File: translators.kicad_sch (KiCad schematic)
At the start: 22 parts

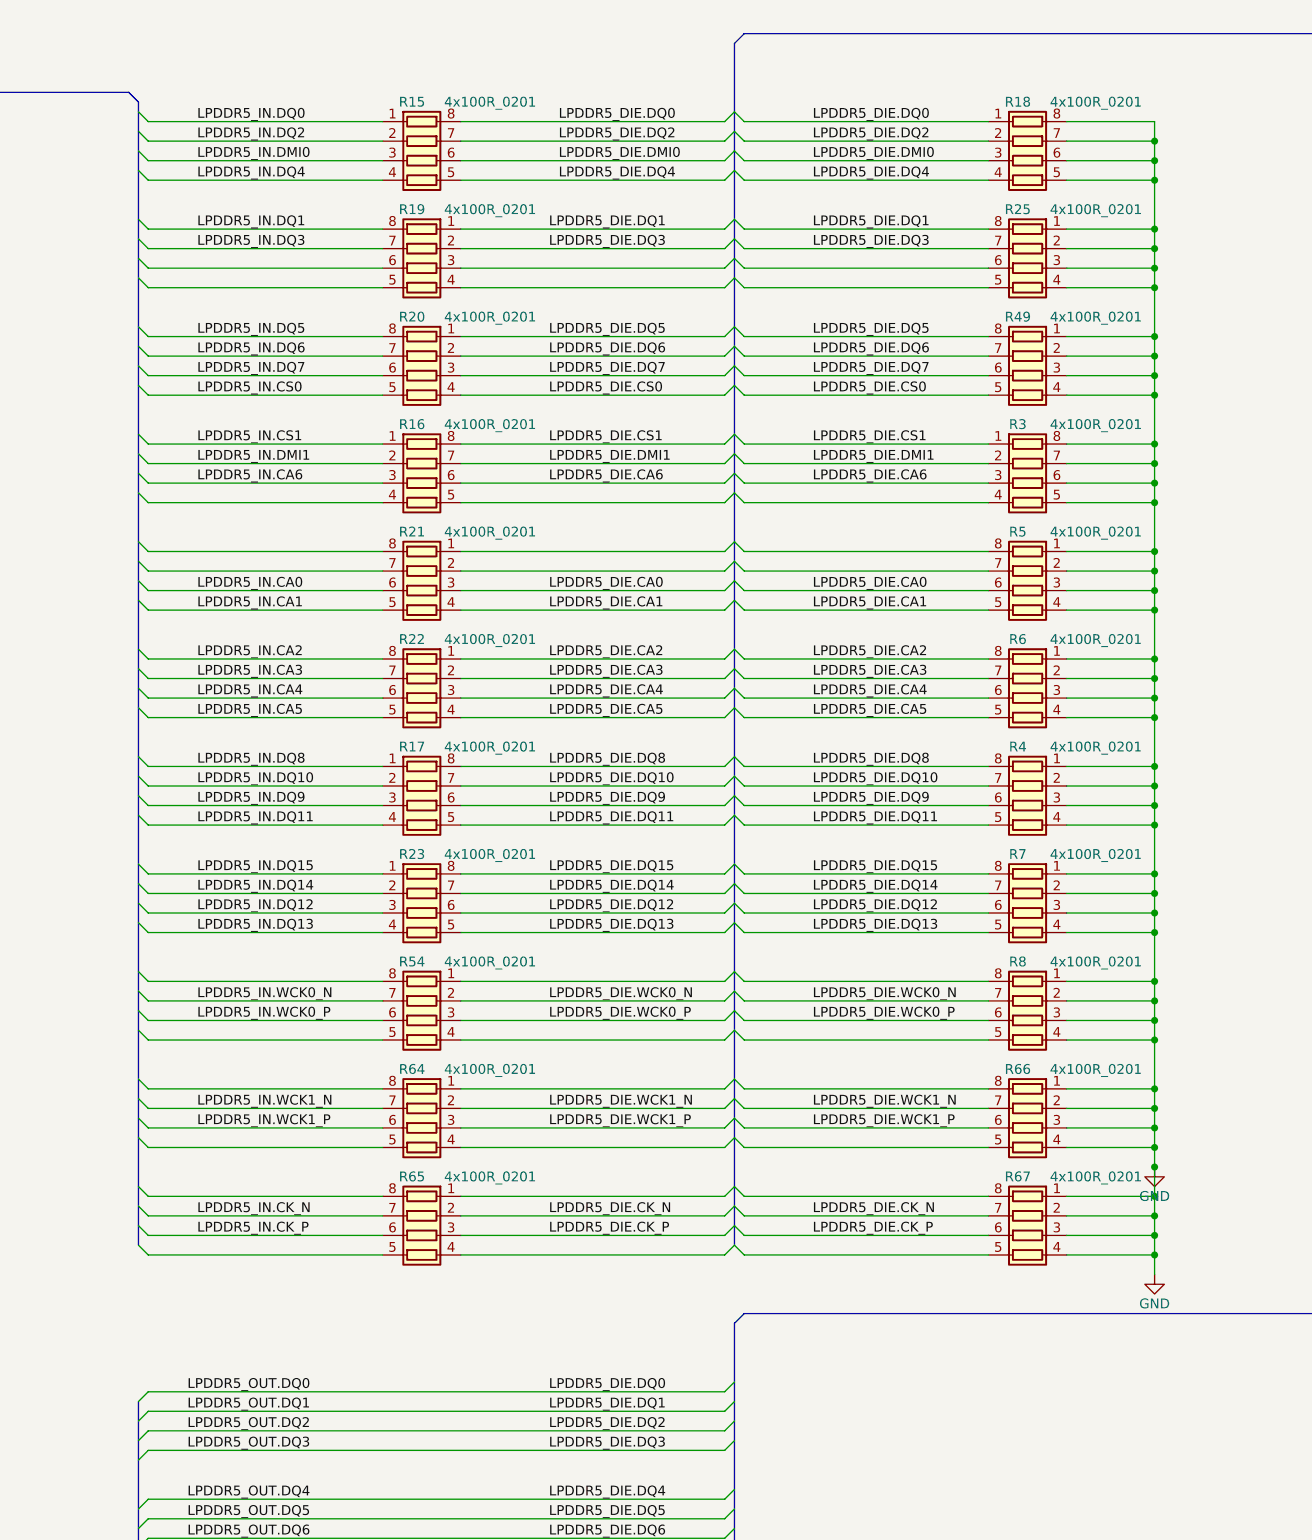
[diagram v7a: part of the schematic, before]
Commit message: [#52835] schematics: replace array resistors with 0402
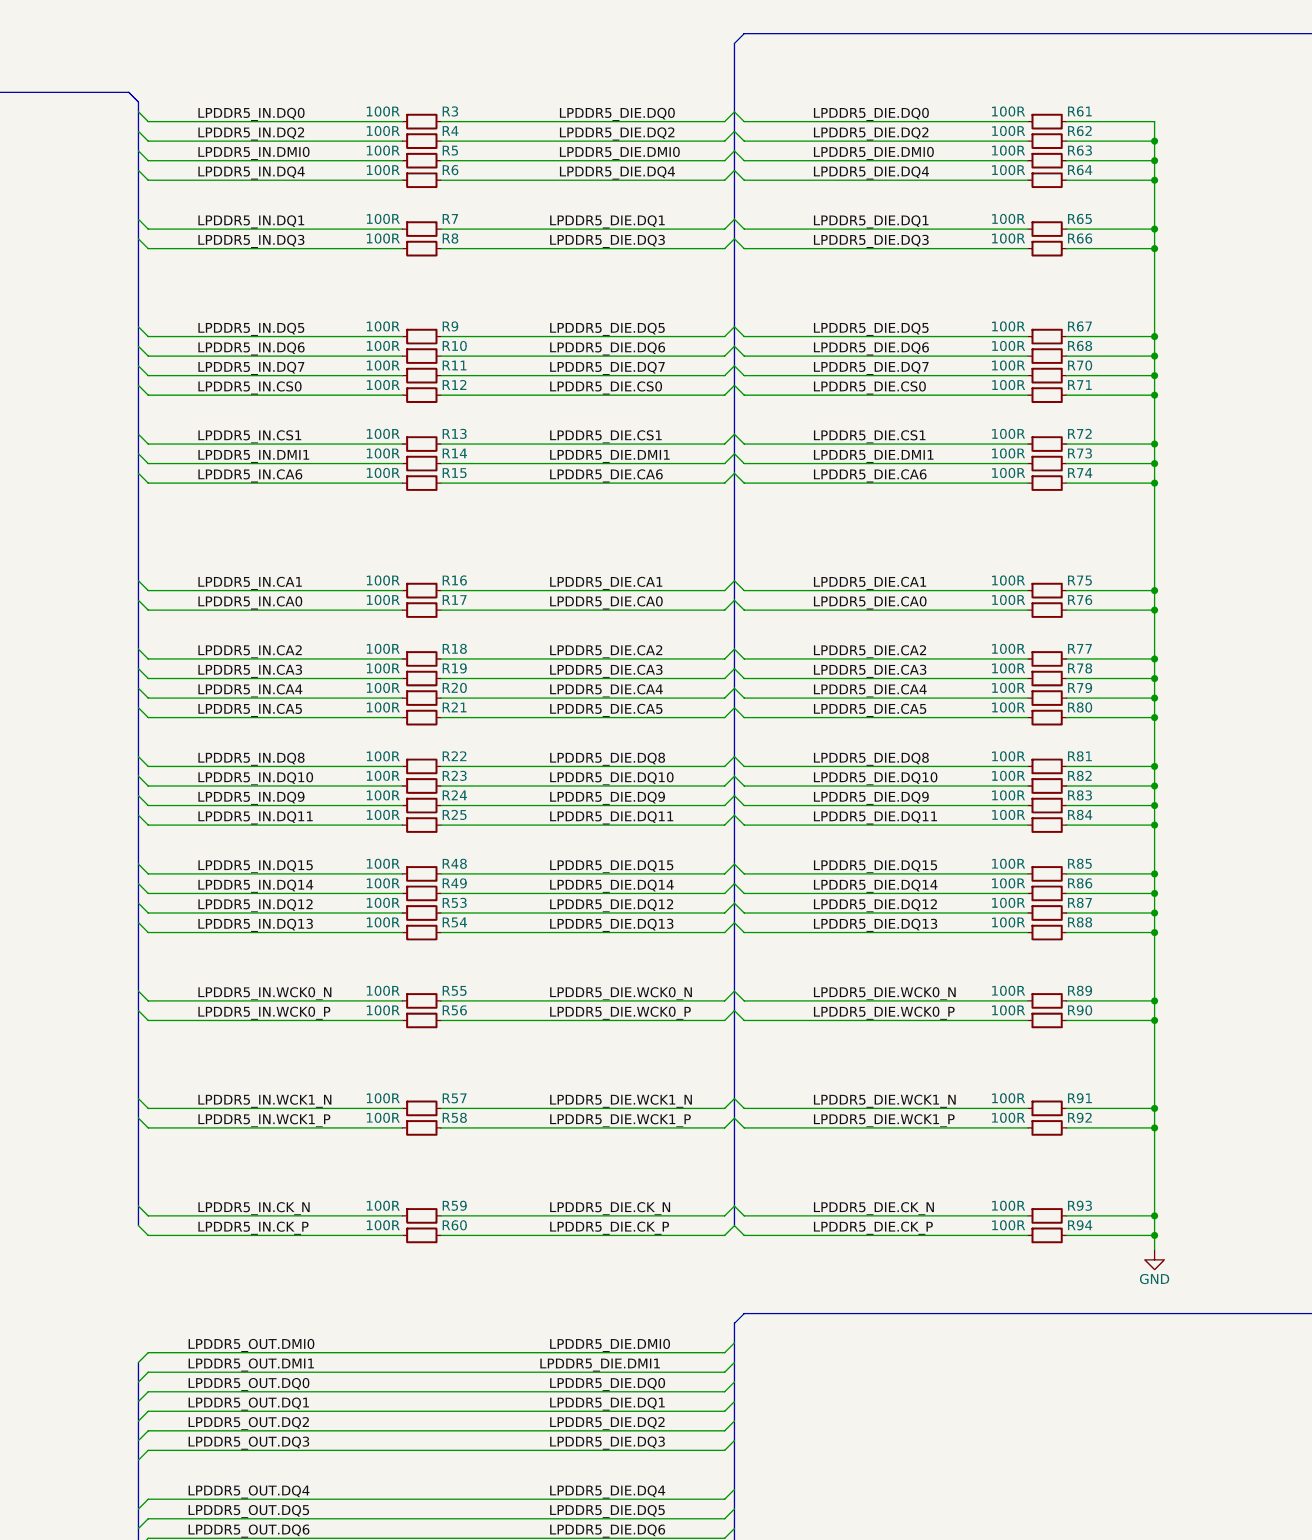
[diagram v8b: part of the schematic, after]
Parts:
- removed R15, R16, R17, R18, R19, R20, R21, R22, R23, R25, R3, R4, R49, R5, R54, R6, R64, R65, R66, R67, R7, R8: 4x100R_0201_array, antmicro-footprints:R_Array_4x0201_Panasonic_EXB18V, symbol antmicroResistorNetworksArrays:4x100R_0201_array
- added R10, R11, R12, R13, R14, R15, R16, R17, R18, R19, R20, R21, R22, R23, R24, R25, R3, R4, R48, R49, R5, R53, R54, R55, R56, R57, R58, R59, R6, R60, R61, R62, R63, R64, R65, R66, R67, R68, R7, R70, R71, R72, R73, R74, R75, R76, R77, R78, R79, R8, R80, R81, R82, R83, R84, R85, R86, R87, R88, R89, R9, R90, R91, R92, R93, R94: R_100R_0402, antmicro-footprints:R_0402_1005Metric, symbol antmicroResistors0402:R_100R_0402
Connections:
- net GND: now also R61.2, R62.2, R63.2, R64.2, R65.2, R66.2, R67.2, R68.2, R70.2, R71.2, R72.2, R73.2, R74.2, R75.2, R76.2, R77.2, R78.2, R79.2, R80.2, R81.2, R82.2, R83.2, R84.2, R85.2, R86.2, R87.2, R88.2, R89.2, R90.2, R91.2, R92.2, R93.2, R94.2
- net LPDDR5_DIE.CA0: now also R17.2, R76.1
- net LPDDR5_DIE.CA1: now also R16.2, R75.1
- net LPDDR5_DIE.CA2: now also R18.2, R77.1
- net LPDDR5_DIE.CA3: now also R19.2, R78.1
- net LPDDR5_DIE.CA4: now also R20.2, R79.1
- net LPDDR5_DIE.CA5: now also R21.2, R80.1
- net LPDDR5_DIE.CA6: now also R15.2, R74.1
- net LPDDR5_DIE.CK_N: now also R59.2, R93.1
- net LPDDR5_DIE.CK_P: now also R60.2, R94.1
- net LPDDR5_DIE.CS0: now also R12.2, R71.1
- net LPDDR5_DIE.CS1: now also R13.2, R72.1
- net LPDDR5_DIE.DMI0: now also R5.2, R63.1
- net LPDDR5_DIE.DMI1: now also R14.2, R73.1
- net LPDDR5_DIE.DQ0: now also R3.2, R61.1
- net LPDDR5_DIE.DQ1: now also R65.1, R7.2
- net LPDDR5_DIE.DQ10: now also R23.2, R82.1
- net LPDDR5_DIE.DQ11: now also R25.2, R84.1
- net LPDDR5_DIE.DQ12: now also R53.2, R87.1
- net LPDDR5_DIE.DQ13: now also R54.2, R88.1
- net LPDDR5_DIE.DQ14: now also R49.2, R86.1
- net LPDDR5_DIE.DQ15: now also R48.2, R85.1
- net LPDDR5_DIE.DQ2: now also R4.2, R62.1
- net LPDDR5_DIE.DQ3: now also R66.1, R8.2
- net LPDDR5_DIE.DQ4: now also R6.2, R64.1
- net LPDDR5_DIE.DQ5: now also R67.1, R9.2
- net LPDDR5_DIE.DQ6: now also R10.2, R68.1
- net LPDDR5_DIE.DQ7: now also R11.2, R70.1
- net LPDDR5_DIE.DQ8: now also R22.2, R81.1
- net LPDDR5_DIE.DQ9: now also R24.2, R83.1
- net LPDDR5_DIE.WCK0_N: now also R55.2, R89.1
- net LPDDR5_DIE.WCK0_P: now also R56.2, R90.1
- net LPDDR5_DIE.WCK1_N: now also R57.2, R91.1
- net LPDDR5_DIE.WCK1_P: now also R58.2, R92.1
- net LPDDR5_IN.CA0: now also R17.1
- net LPDDR5_IN.CA1: now also R16.1
- net LPDDR5_IN.CA2: now also R18.1
- net LPDDR5_IN.CA3: now also R19.1
- net LPDDR5_IN.CA4: now also R20.1
- net LPDDR5_IN.CA5: now also R21.1
- net LPDDR5_IN.CA6: now also R15.1
- net LPDDR5_IN.CK_N: now also R59.1
- net LPDDR5_IN.CK_P: now also R60.1
- net LPDDR5_IN.CS0: now also R12.1
- net LPDDR5_IN.CS1: now also R13.1
- net LPDDR5_IN.DMI0: now also R5.1
- net LPDDR5_IN.DMI1: now also R14.1
- net LPDDR5_IN.DQ0: now also R3.1
- net LPDDR5_IN.DQ1: now also R7.1
- net LPDDR5_IN.DQ10: now also R23.1
- net LPDDR5_IN.DQ11: now also R25.1
- net LPDDR5_IN.DQ12: now also R53.1
- net LPDDR5_IN.DQ13: now also R54.1
- net LPDDR5_IN.DQ14: now also R49.1
- net LPDDR5_IN.DQ15: now also R48.1
- net LPDDR5_IN.DQ2: now also R4.1
- net LPDDR5_IN.DQ3: now also R8.1
- net LPDDR5_IN.DQ4: now also R6.1
- net LPDDR5_IN.DQ5: now also R9.1
- net LPDDR5_IN.DQ6: now also R10.1
- net LPDDR5_IN.DQ7: now also R11.1
- net LPDDR5_IN.DQ8: now also R22.1
- net LPDDR5_IN.DQ9: now also R24.1
- net LPDDR5_IN.WCK0_N: now also R55.1
- net LPDDR5_IN.WCK0_P: now also R56.1
- net LPDDR5_IN.WCK1_N: now also R57.1
- net LPDDR5_IN.WCK1_P: now also R58.1
